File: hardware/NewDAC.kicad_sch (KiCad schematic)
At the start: 59 parts, among them J1 PJ-322, U1 PCM1795, U14 OPA1656, U15 OPA1656, U6 LM4562, U7 LM4562

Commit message: some changes
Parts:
- added D11, D12: PESD3V3L1BA, rlib_passive:D_SOD-323F, symbol rlib_passive:PESD3V3L1BA
- added TP20, TP21: TestPoint, symbol Connector:TestPoint
- C104, C105, C108, C109, C80, C81, C90, C91: footprint (none) -> rlib_passive:T491A106K010AT; Mnfct.  partnumber (none) -> T491A106K010AT
- C79: value C -> 100n
- C84, C87, C88, C89: value C_Pol -> 10u; footprint (none) -> rlib_passive:T491A106K010AT; Mnfct.  partnumber (none) -> T491A106K010AT
- C85, C86: value C -> 10u; footprint (none) -> rlib_passive:T491A106K010AT; Mnfct.  partnumber (none) -> T491A106K010AT
- C94, C95, C96, C97: value C -> 2.2n
- C98, C99: value C -> 27n
- R51, R52, R53, R54: value R -> 820
- R66, R67: value 220 -> 50
- U1: footprint (none) -> rlib_ic:SSOP-28_5.3x10.2mm_P0.65mm
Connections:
- net GNDA: now also J1.1, D11.1 (A1), D12.1 (A1)
- net at J1.4, R67.2: now also D11.2 (A2), TP21.1
- net at R66.2: now also J1.3, D12.2 (A2), TP20.1; no longer J1.2
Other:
- moved on the sheet: C104, C105, C106, C107, C108, C109, C110, C111, C80, C81, C82, C83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

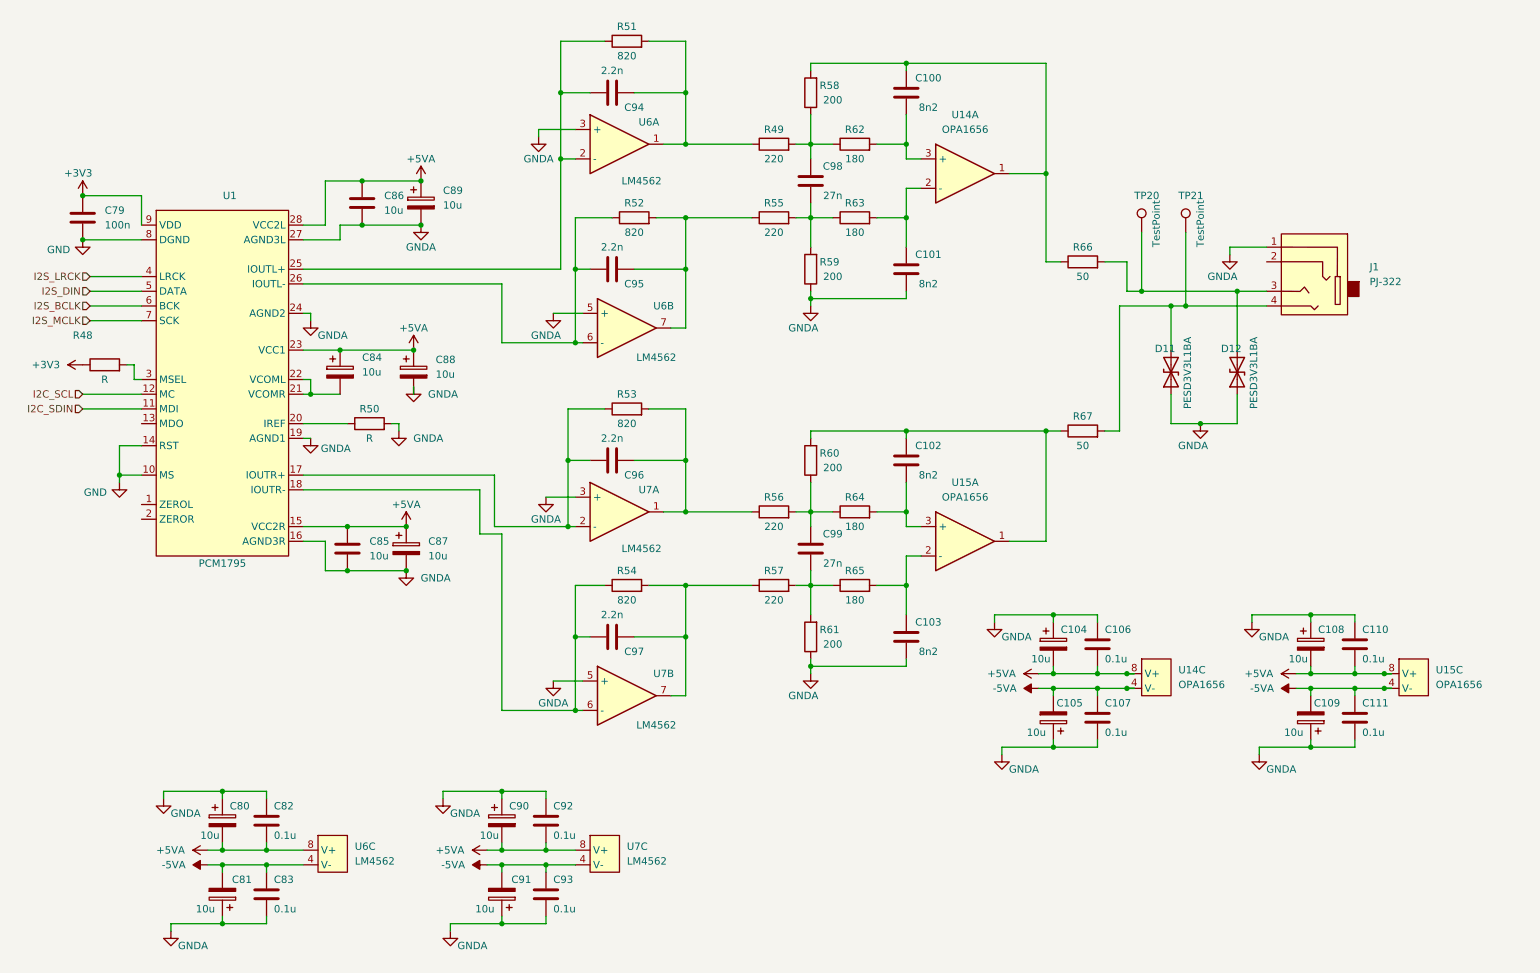
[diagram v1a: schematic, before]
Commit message: new power list added
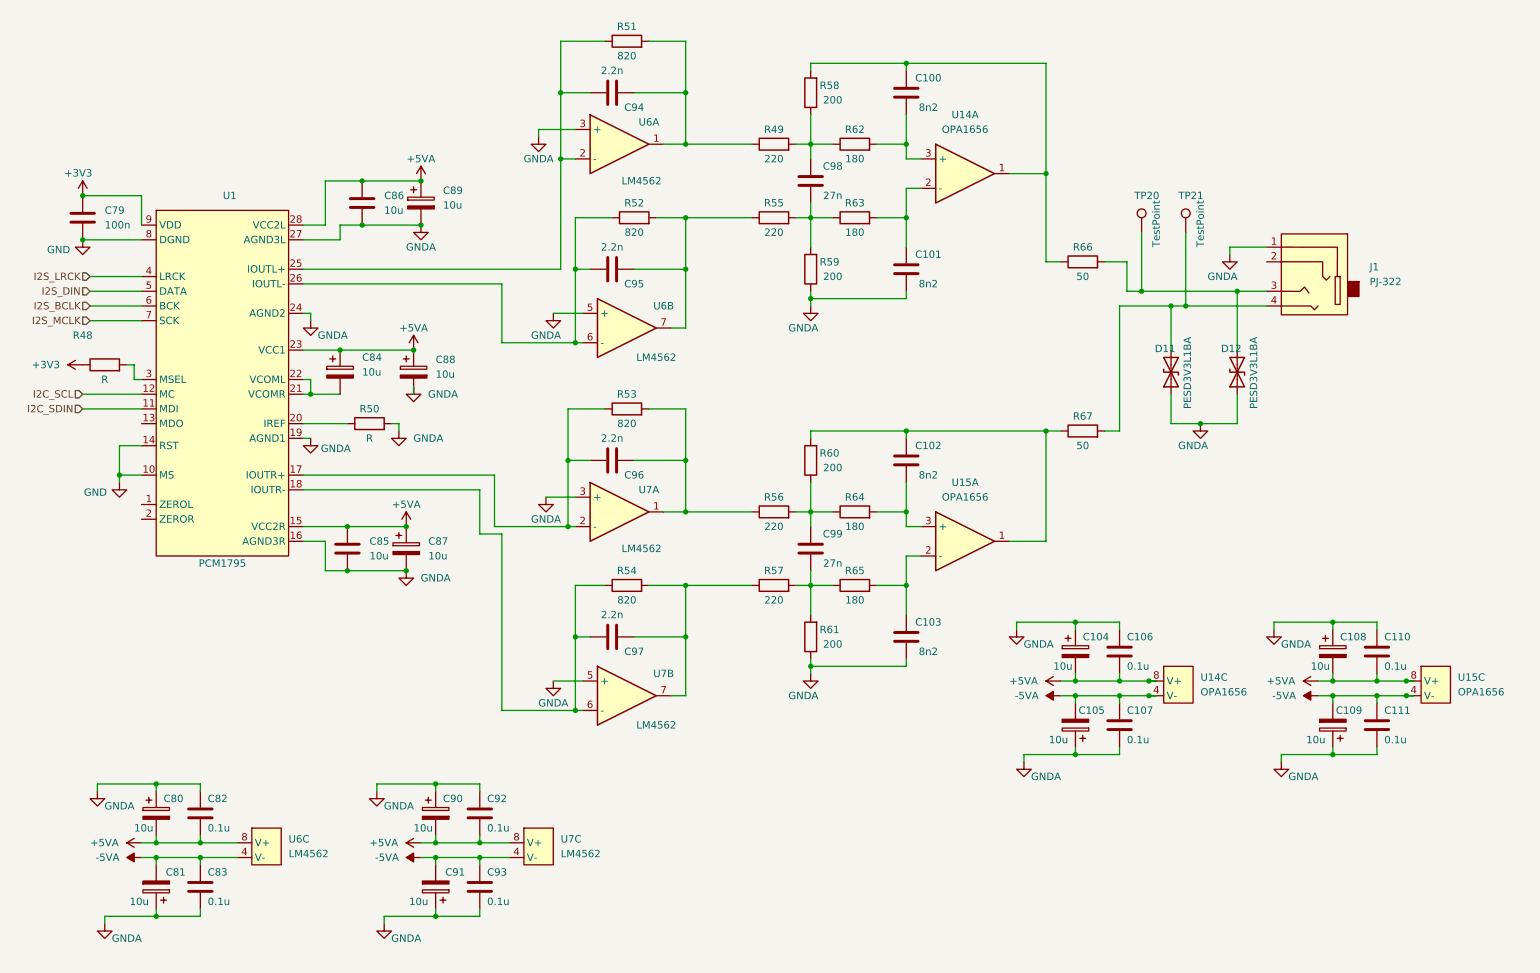
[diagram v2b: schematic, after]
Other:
- moved on the sheet: C104, C105, C106, C107, C108, C109, C110, C111, C80, C81, C82, C83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

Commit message: some chnages
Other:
- moved on the sheet: C100, C101, C102, C103, C104, C105, C106, C107, C108, C109, C110, C111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
